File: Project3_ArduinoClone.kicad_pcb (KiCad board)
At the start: 2 copper layers, 40.1 x 26.4 mm, 17 parts, among them J1 Serial, J2 Digital pins, J3 ICSP, J4 I2C, U1 24LC1025, U2 24LC1025, U3 DS1337_v1, U4 ATMEGA328P-AU, Y1 Crystal 32 MHz, Y2 Crystal 16 MHz

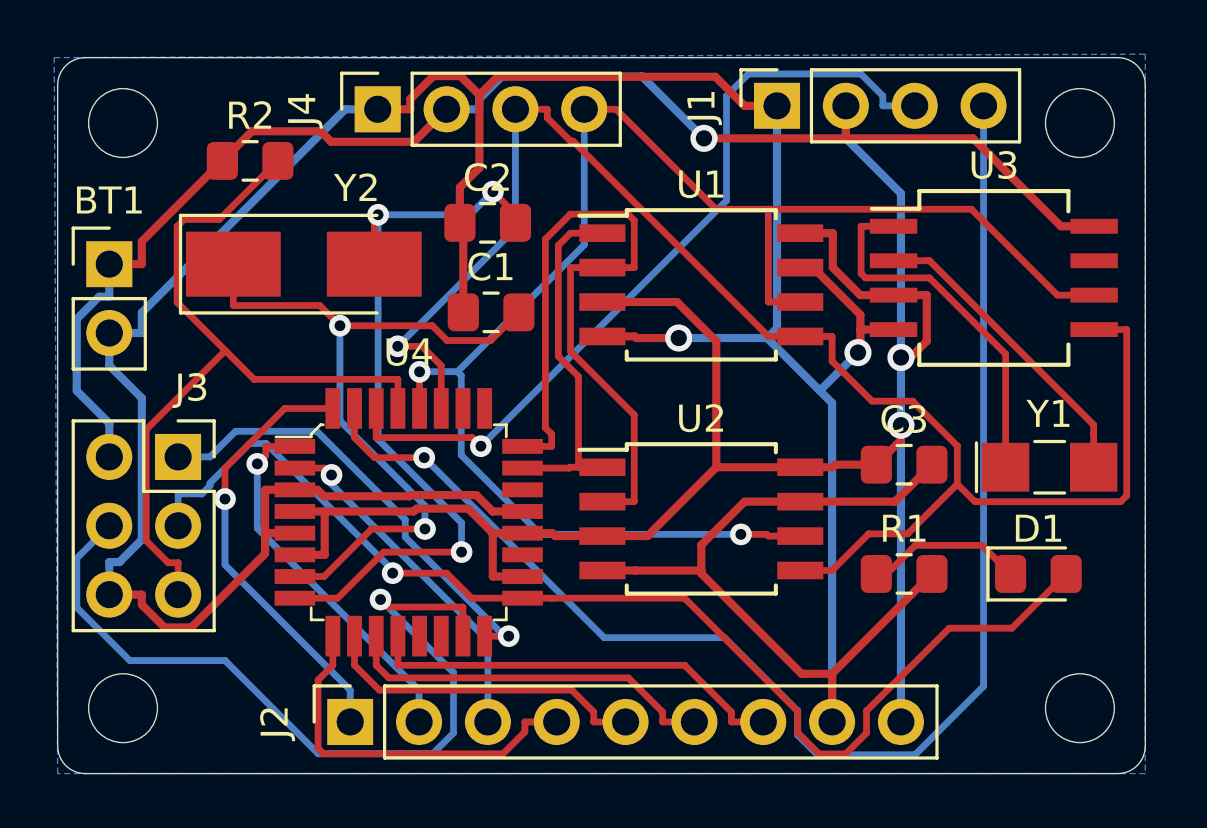
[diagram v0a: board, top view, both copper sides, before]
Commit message: Add silkscreen text
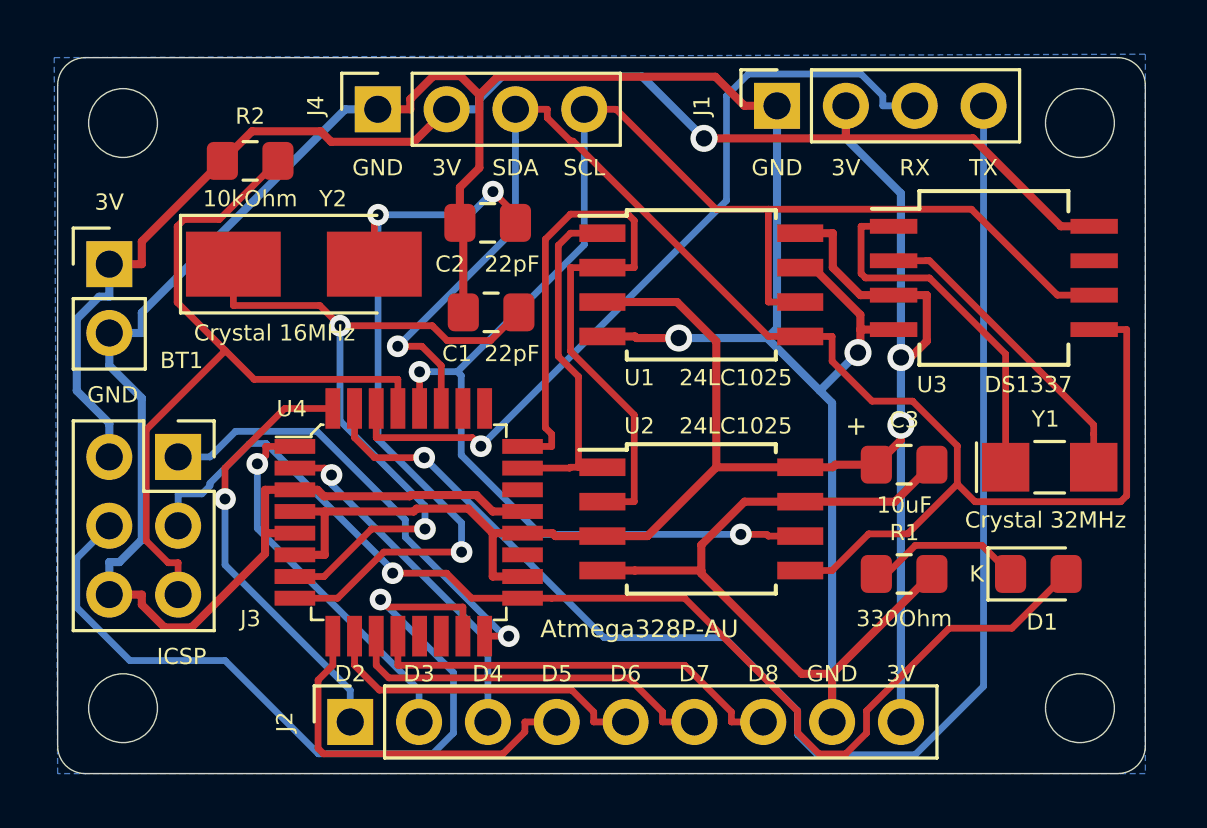
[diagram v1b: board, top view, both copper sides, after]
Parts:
- U3: value DS1337_v1 -> DS1337
- Y1: value Crystal 32 MHz -> Crystal 32MHz
- Y2: value Crystal 16 MHz -> Crystal 16MHz
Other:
- board text added: "+"
- board text added: "3V"
- board text added: "Atmega328P-AU"
- board text added: "D2"
- board text added: "D3"
- board text added: "D4"
- board text added: "D5"
- board text added: "D6"
- board text added: "D7"
- board text added: "D8"
- board text added: "GND"
- board text added: "K"
- board text added: "RX"
- board text added: "SCL"
- board text added: "SDA"
- board text added: "TX"

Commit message: Final silkscreen, generate gerbers
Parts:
- added REF**: OSHW-Logo_5.7x6mm_SilkScreen, Symbol:OSHW-Logo_5.7x6mm_SilkScreen, B.Cu at (97.5, 137.8)
- added REF**: KiCad-Logo2_5mm_SilkScreen, Symbol:KiCad-Logo2_5mm_SilkScreen, B.Cu at (110.4, 138.0)
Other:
- board text added: "Arduino Clone -EEPROM 2MB -RTC -3V or 3V3 powered"
- board text added: "Designed by Pablo Roig"
